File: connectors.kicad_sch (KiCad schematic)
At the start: 31 parts, among them J1 Conn_01x02, J2 USB_B_Micro, J3 Conn_01x04, J4 Conn_01x04, J5 Conn_01x04, J6 Conn_01x04, J7 Conn_01x04, J8 Conn_01x04, J9 Conn_02x05_Odd_Even, U4 USBLC6-2SC6

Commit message: updated schematic
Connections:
- net TIM3_CH4: now reaches R20.1
- net USART1_RX: now reaches R18.1
- net TIM2_CH4: now reaches R22.1
- net USART1_TX: now reaches R17.1
- net I2C1_SCL: now reaches R15.1
- net ADC1_IN2: now reaches R23.1
- net ADC1_IN3: now reaches R24.1
- net ADC1_IN1: now reaches R26.1
- net TIM2_CH3: now reaches R21.1
- net TIM3_CH3: now reaches R19.1
- net ADC1_IN0: now reaches R25.1
- net I2C1_SDA: now reaches R16.1
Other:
- moved on the sheet: J1
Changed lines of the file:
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@@
     (stroke (width 0) (type default) (color 0 0 0 0))
   )
-  (wire (pts (xy 38.1 58.42) (xy 38.1 55.88))
+  (wire (pts (xy 22.86 57.15) (xy 22.86 54.61))
     (stroke (width 0) (type default) (color 0 0 0 0))
   )
@@
     (stroke (width 0) (type default) (color 0 0 0 0))
   )
-  (wire (pts (xy 38.1 50.8) (xy 38.1 53.34))
+  (wire (pts (xy 22.86 49.53) (xy 22.86 52.07))
     (stroke (width 0) (type default) (color 0 0 0 0))
   )
@@
     (stroke (width 0) (type default) (color 0 0 0 0))
   )
+  (global_label "I2C1_SCL" (shape input) (at 69.85 54.61 180) (fields_autoplaced)
+    (effects (font (size 1.27 1.27)) (justify right))
+    (property "Intersheet References" "${INTERSHEET_REFS}" (id 0) (at 58.6679 54.5306 0)
+      (effects (font (size 1.27 1.27)) (justify right) hide)
+    )
+  )
+  (global_label "I2C1_SDA" (shape input) (at 69.85 57.15 180) (fields_autoplaced)
+    (effects (font (size 1.27 1.27)) (justify right))
+    (property "Intersheet References" "${INTERSHEET_REFS}" (id 0) (at 58.6074 57.0706 0)
+      (effects (font (size 1.27 1.27)) (justify right) hide)
+    )
+  )
   (global_label "USB_D-" (shape input) (at 116.84 139.7 180) (fields_autoplaced)
     (effects (font (size 1.27 1.27)) (justify right))
     (property "Intersheet References" "${INTERSHEET_REFS}" (id 0) (at 106.8069 139.6206 0)
+      (effects (font (size 1.27 1.27)) (justify right) hide)
+    )
+  )
+  (global_label "ADC1_IN3" (shape input) (at 157.48 92.71 180) (fields_autoplaced)
+    (effects (font (size 1.27 1.27)) (justify right))
+    (property "Intersheet References" "${INTERSHEET_REFS}" (id 0) (at 146.1164 92.6306 0)
       (effects (font (size 1.27 1.27)) (justify right) hide)
     )
@@
     )
   )
+  (global_label "ADC1_IN2" (shape input) (at 157.48 90.17 180) (fields_autoplaced)
+    (effects (font (size 1.27 1.27)) (justify right))
+    (property "Intersheet References" "${INTERSHEET_REFS}" (id 0) (at 146.1164 90.0906 0)
+      (effects (font (size 1.27 1.27)) (justify right) hide)
+    )
+  )
+  (global_label "USART1_RX" (shape input) (at 69.85 93.98 180) (fields_autoplaced)
+    (effects (font (size 1.27 1.27)) (justify right))
+    (property "Intersheet References" "${INTERSHEET_REFS}" (id 0) (at 56.914 93.9006 0)
+      (effects (font (size 1.27 1.27)) (justify right) hide)
+    )
+  )
+  (global_label "TIM3_CH3" (shape input) (at 113.03 91.44 180) (fields_autoplaced)
+    (effects (font (size 1.27 1.27)) (justify right))
+    (property "Intersheet References" "${INTERSHEET_REFS}" (id 0) (at 101.6059 91.3606 0)
+      (effects (font (size 1.27 1.27)) (justify right) hide)
+    )
+  )
   (global_label "NRST" (shape input) (at 257.81 78.74 0) (fields_autoplaced)
     (effects (font (size 1.27 1.27)) (justify left))
@@
     )
   )
+  (global_label "ADC1_IN0" (shape input) (at 158.75 54.61 180) (fields_autoplaced)
+    (effects (font (size 1.27 1.27)) (justify right))
+    (property "Intersheet References" "${INTERSHEET_REFS}" (id 0) (at 147.3864 54.5306 0)
+      (effects (font (size 1.27 1.27)) (justify right) hide)
+    )
+  )
+  (global_label "USART1_TX" (shape input) (at 69.85 91.44 180) (fields_autoplaced)
+    (effects (font (size 1.27 1.27)) (justify right))
+    (property "Intersheet References" "${INTERSHEET_REFS}" (id 0) (at 57.2164 91.3606 0)
+      (effects (font (size 1.27 1.27)) (justify right) hide)
+    )
+  )
   (global_label "SWDIO" (shape input) (at 257.81 68.58 0) (fields_autoplaced)
     (effects (font (size 1.27 1.27)) (justify left))
@@
     )
   )
+  (global_label "TIM3_CH4" (shape input) (at 113.03 93.98 180) (fields_autoplaced)
+    (effects (font (size 1.27 1.27)) (justify right))
+    (property "Intersheet References" "${INTERSHEET_REFS}" (id 0) (at 101.6059 93.9006 0)
+      (effects (font (size 1.27 1.27)) (justify right) hide)
+    )
+  )
+  (global_label "ADC1_IN1" (shape input) (at 158.75 57.15 180) (fields_autoplaced)
+    (effects (font (size 1.27 1.27)) (justify right))
+    (property "Intersheet References" "${INTERSHEET_REFS}" (id 0) (at 147.3864 57.0706 0)
+      (effects (font (size 1.27 1.27)) (justify right) hide)
+    )
+  )
+  (global_label "TIM2_CH3" (shape input) (at 114.3 53.34 180) (fields_autoplaced)
+    (effects (font (size 1.27 1.27)) (justify right))
+    (property "Intersheet References" "${INTERSHEET_REFS}" (id 0) (at 102.8759 53.2606 0)
+      (effects (font (size 1.27 1.27)) (justify right) hide)
+    )
+  )
+  (global_label "TIM2_CH4" (shape input) (at 114.3 55.88 180) (fields_autoplaced)
+    (effects (font (size 1.27 1.27)) (justify right))
+    (property "Intersheet References" "${INTERSHEET_REFS}" (id 0) (at 102.8759 55.8006 0)
+      (effects (font (size 1.27 1.27)) (justify right) hide)
+    )
+  )
   (global_label "SWO" (shape input) (at 257.81 73.66 0) (fields_autoplaced)
     (effects (font (size 1.27 1.27)) (justify left))
@@
     (pin "1")
   )
-  (symbol (lib_id "power:VCC") (at 38.1 50.8 0) (unit 1)
-    (in_bom yes) (on_board yes) (fields_autoplaced)
-    (property "Reference" "#PWR030" (id 0) (at 38.1 54.61 0)
-      (effects (font (size 1.27 1.27)) hide)
-    )
-    (property "Value" "VCC" (id 1) (at 38.1 45.72 0))
-    (property "Footprint" "" (id 2) (at 38.1 50.8 0)
-      (effects (font (size 1.27 1.27)) hide)
-    )
-    (property "Datasheet" "" (id 3) (at 38.1 50.8 0)
+  (symbol (lib_id "power:VCC") (at 22.86 49.53 0) (unit 1)
+    (in_bom yes) (on_board yes) (fields_autoplaced)
+    (property "Reference" "#PWR030" (id 0) (at 22.86 53.34 0)
+      (effects (font (size 1.27 1.27)) hide)
+    )
+    (property "Value" "VCC" (id 1) (at 22.86 44.45 0))
+    (property "Footprint" "" (id 2) (at 22.86 49.53 0)
+      (effects (font (size 1.27 1.27)) hide)
+    )
+    (property "Datasheet" "" (id 3) (at 22.86 49.53 0)
       (effects (font (size 1.27 1.27)) hide)
     )
@@
     (pin "1")
   )
-  (symbol (lib_id "Connector_Generic:Conn_01x02") (at 43.18 53.34 0) (unit 1)
-    (in_bom yes) (on_board yes) (fields_autoplaced)
-    (property "Reference" "J1" (id 0) (at 45.72 53.3399 0)
-      (effects (font (size 1.27 1.27)) (justify left))
-    )
-    (property "Value" "Conn_01x02" (id 1) (at 45.72 55.8799 0)
-      (effects (font (size 1.27 1.27)) (justify left))
-    )
-    (property "Footprint" "" (id 2) (at 43.18 53.34 0)
-      (effects (font (size 1.27 1.27)) hide)
-    )
-    (property "Datasheet" "~" (id 3) (at 43.18 53.34 0)
+  (symbol (lib_id "Connector_Generic:Conn_01x02") (at 27.94 52.07 0) (unit 1)
+    (in_bom yes) (on_board yes) (fields_autoplaced)
+    (property "Reference" "J1" (id 0) (at 30.48 52.0699 0)
+      (effects (font (size 1.27 1.27)) (justify left))
+    )
+    (property "Value" "Conn_01x02" (id 1) (at 30.48 54.6099 0)
+      (effects (font (size 1.27 1.27)) (justify left))
+    )
+    (property "Footprint" "" (id 2) (at 27.94 52.07 0)
+      (effects (font (size 1.27 1.27)) hide)
+    )
+    (property "Datasheet" "~" (id 3) (at 27.94 52.07 0)
       (effects (font (size 1.27 1.27)) hide)
     )
@@
     (pin "1")
   )
-  (symbol (lib_id "power:GND") (at 38.1 58.42 0) (unit 1)
-    (in_bom yes) (on_board yes) (fields_autoplaced)
-    (property "Reference" "#PWR031" (id 0) (at 38.1 64.77 0)
-      (effects (font (size 1.27 1.27)) hide)
-    )
-    (property "Value" "GND" (id 1) (at 38.1 63.5 0))
-    (property "Footprint" "" (id 2) (at 38.1 58.42 0)
-      (effects (font (size 1.27 1.27)) hide)
-    )
-    (property "Datasheet" "" (id 3) (at 38.1 58.42 0)
-      (effects (font (size 1.27 1.27)) hide)
-    )
+  (symbol (lib_id "power:GND") (at 22.86 57.15 0) (unit 1)
+    (in_bom yes) (on_board yes) (fields_autoplaced)
+    (property "Reference" "#PWR031" (id 0) (at 22.86 63.5 0)
+      (effects (font (size 1.27 1.27)) hide)
+    )
+    (property "Value" "GND" (id 1) (at 22.86 62.23 0))
+    (property "Footprint" "" (id 2) (at 22.86 57.15 0)
+      (effects (font (size 1.27 1.27)) hide)
+    )
+    (property "Datasheet" "" (id 3) (at 22.86 57.15 0)
+      (effects (font (size 1.27 1.27)) hide)
+    )

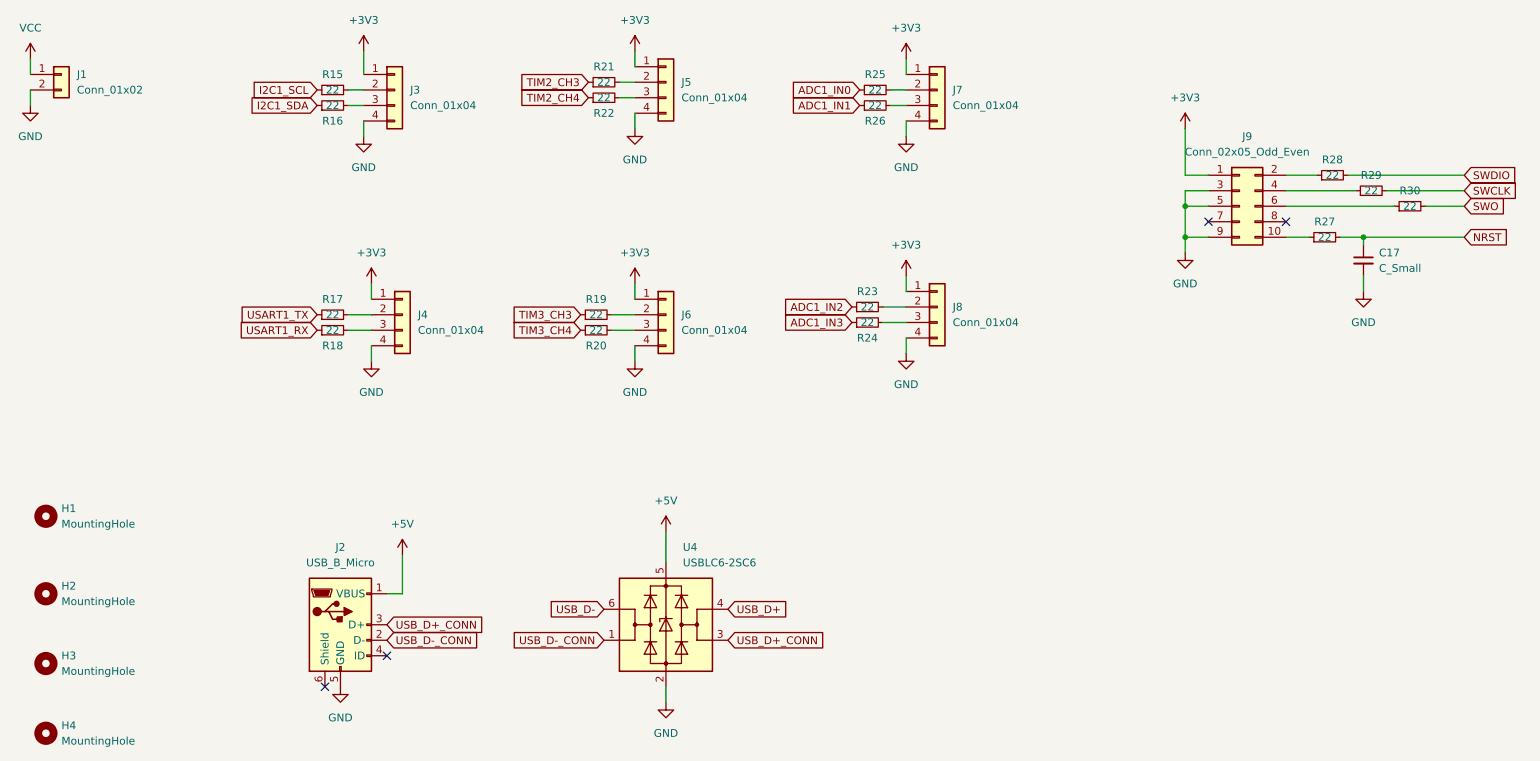
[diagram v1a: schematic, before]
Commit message: updated and parts placement
basic parts placement
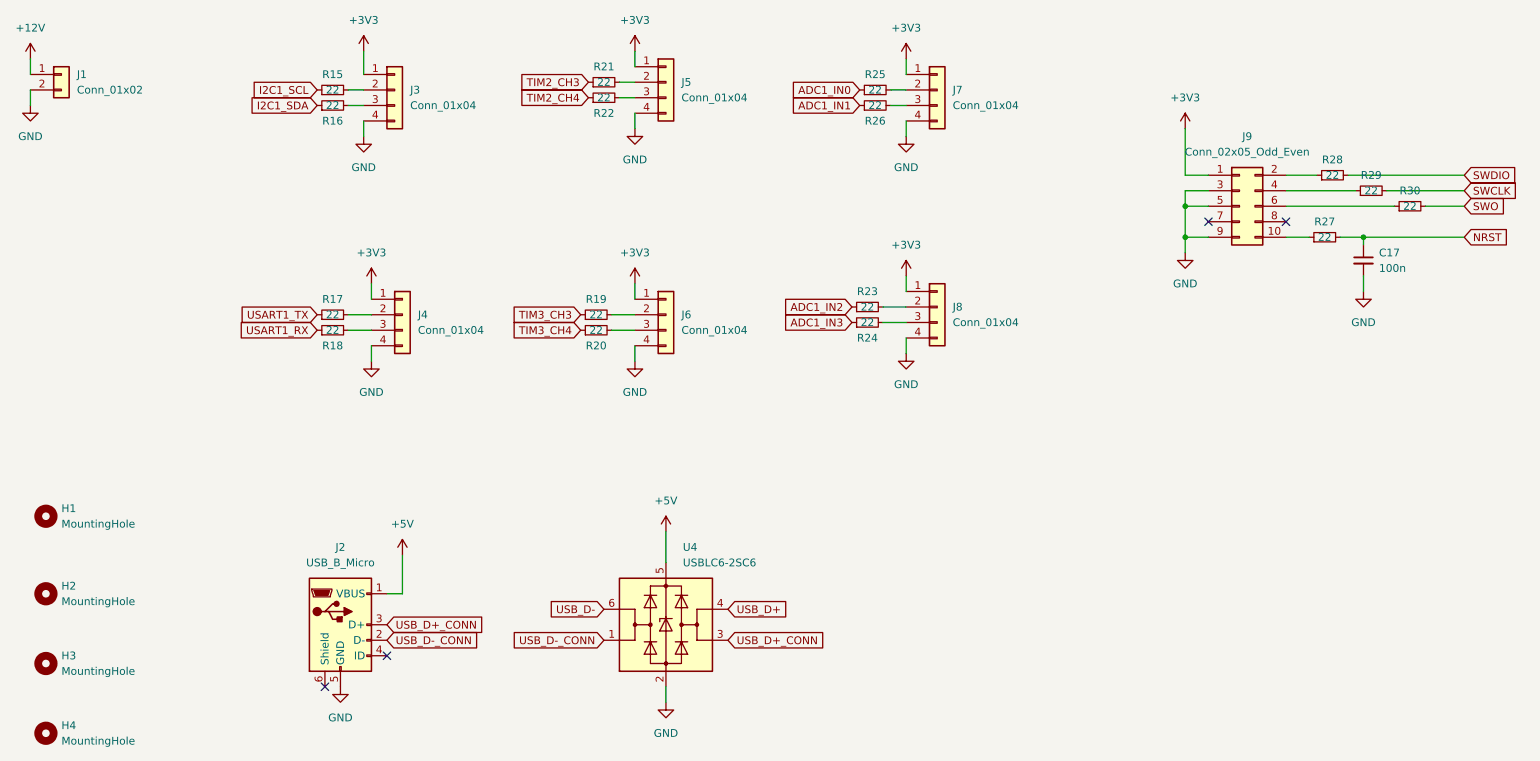
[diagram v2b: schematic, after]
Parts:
- C17: value C_Small -> 100n; footprint (none) -> Capacitor_SMD:C_0402_1005Metric
- H1, H2, H3, H4: footprint (none) -> MountingHole:MountingHole_3.2mm_M3_Pad
- J1: footprint (none) -> Connector_Molex:Molex_PicoBlade_53048-0210_1x02_P1.25mm_Horizontal
- J2: footprint (none) -> Connector_USB:USB_Micro-B_Wuerth_629105150521
- J3, J4, J5, J6, J7, J8: footprint (none) -> Connector_Molex:Molex_PicoBlade_53048-0410_1x04_P1.25mm_Horizontal
- J9: footprint (none) -> Connector_PinHeader_1.27mm:PinHeader_2x05_P1.27mm_Vertical_SMD
- R15, R16, R17, R18, R19, R20, R21, R22, R23, R24, R25, R26, R27, R28, R29, R30: footprint (none) -> Resistor_SMD:R_0402_1005Metric
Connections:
- net VCC renamed +12V
